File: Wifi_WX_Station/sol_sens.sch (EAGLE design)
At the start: 9 parts, among them IC1 MAX4330, U1 CPC1822

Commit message: updated BOM with all prices- As Checked in to BATCH PCB
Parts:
- C1: value 22nF -> 0.1uf
- C2: value 100nF -> 0.1uF
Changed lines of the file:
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@@
 <part name="R2" library="rcl" deviceset="R-US_" device="R0805" value="47K"/>
 <part name="IC1" library="Stofer" deviceset="MAX4330" device=""/>
-<part name="C2" library="rcl" deviceset="C-US" device="C0805" value="100nF"/>
-<part name="C1" library="rcl" deviceset="C-US" device="C0805" value="22nF"/>
+<part name="C2" library="rcl" deviceset="C-US" device="C0805" value="0.1uF"/>
+<part name="C1" library="rcl" deviceset="C-US" device="C0805" value="0.1uf"/>
 <part name="TP1" library="Stofer" deviceset="TP" device="B1,27"/>
 <part name="TP2" library="Stofer" deviceset="TP" device="B1,27"/>

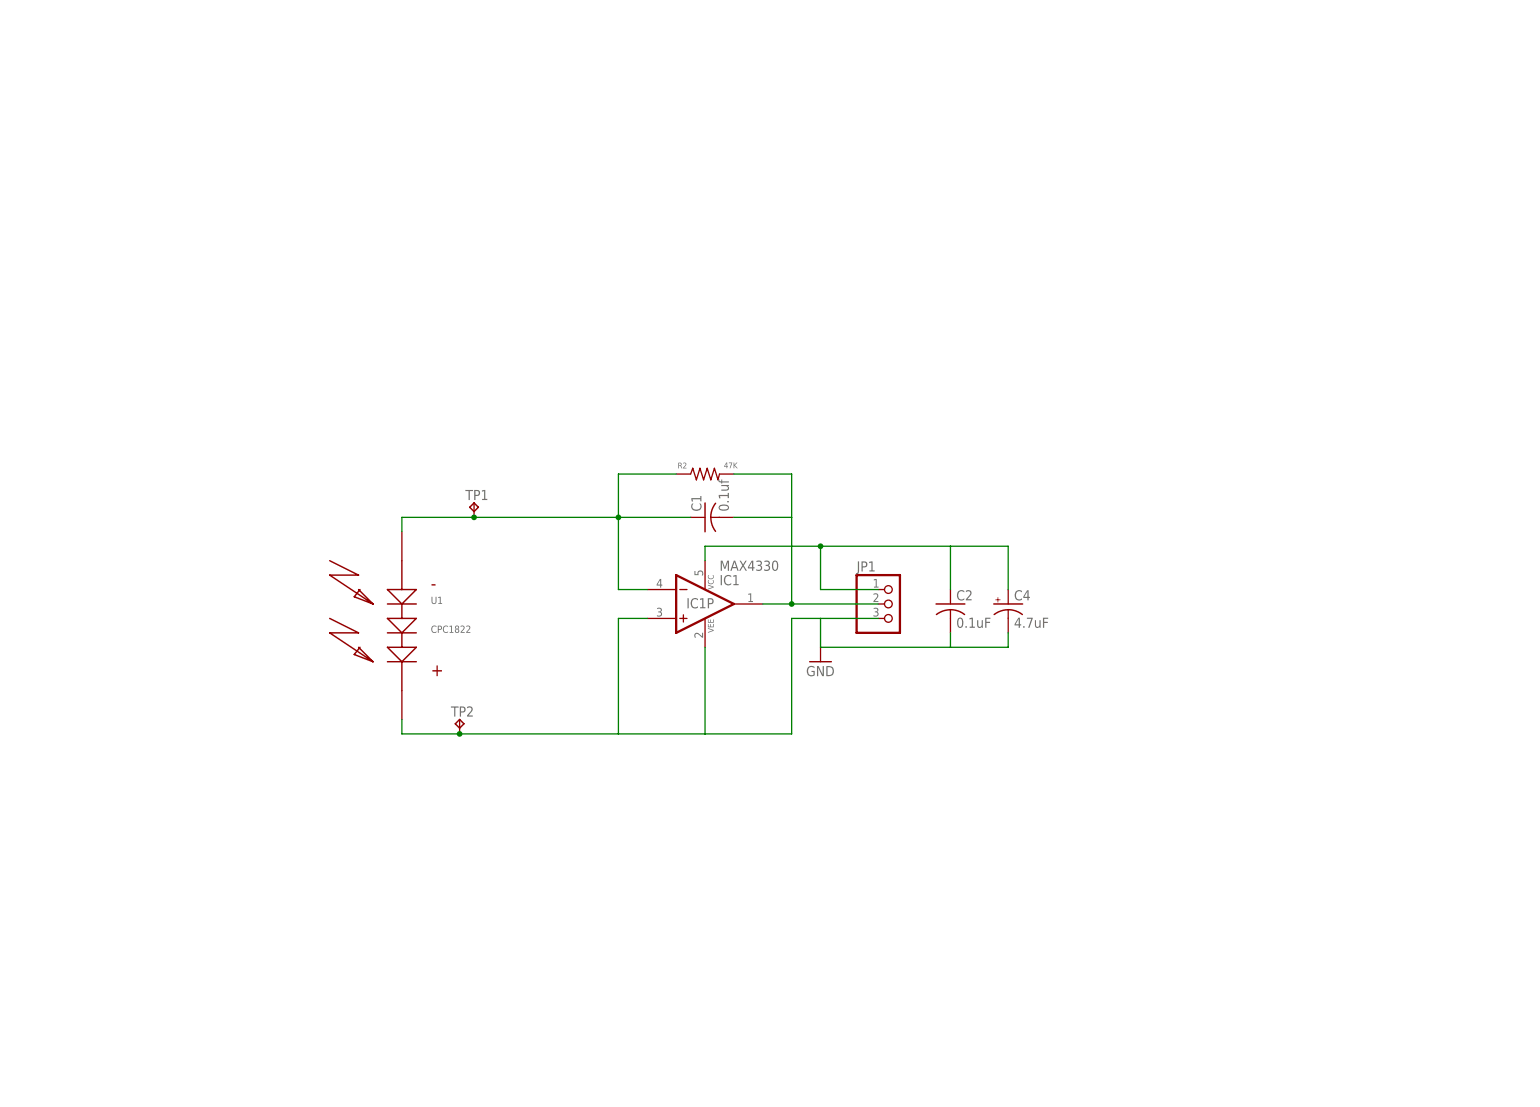
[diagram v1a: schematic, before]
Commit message: Added multiple new boards - H-pwrdist- Insp_Wind_enc, 5040 etc..
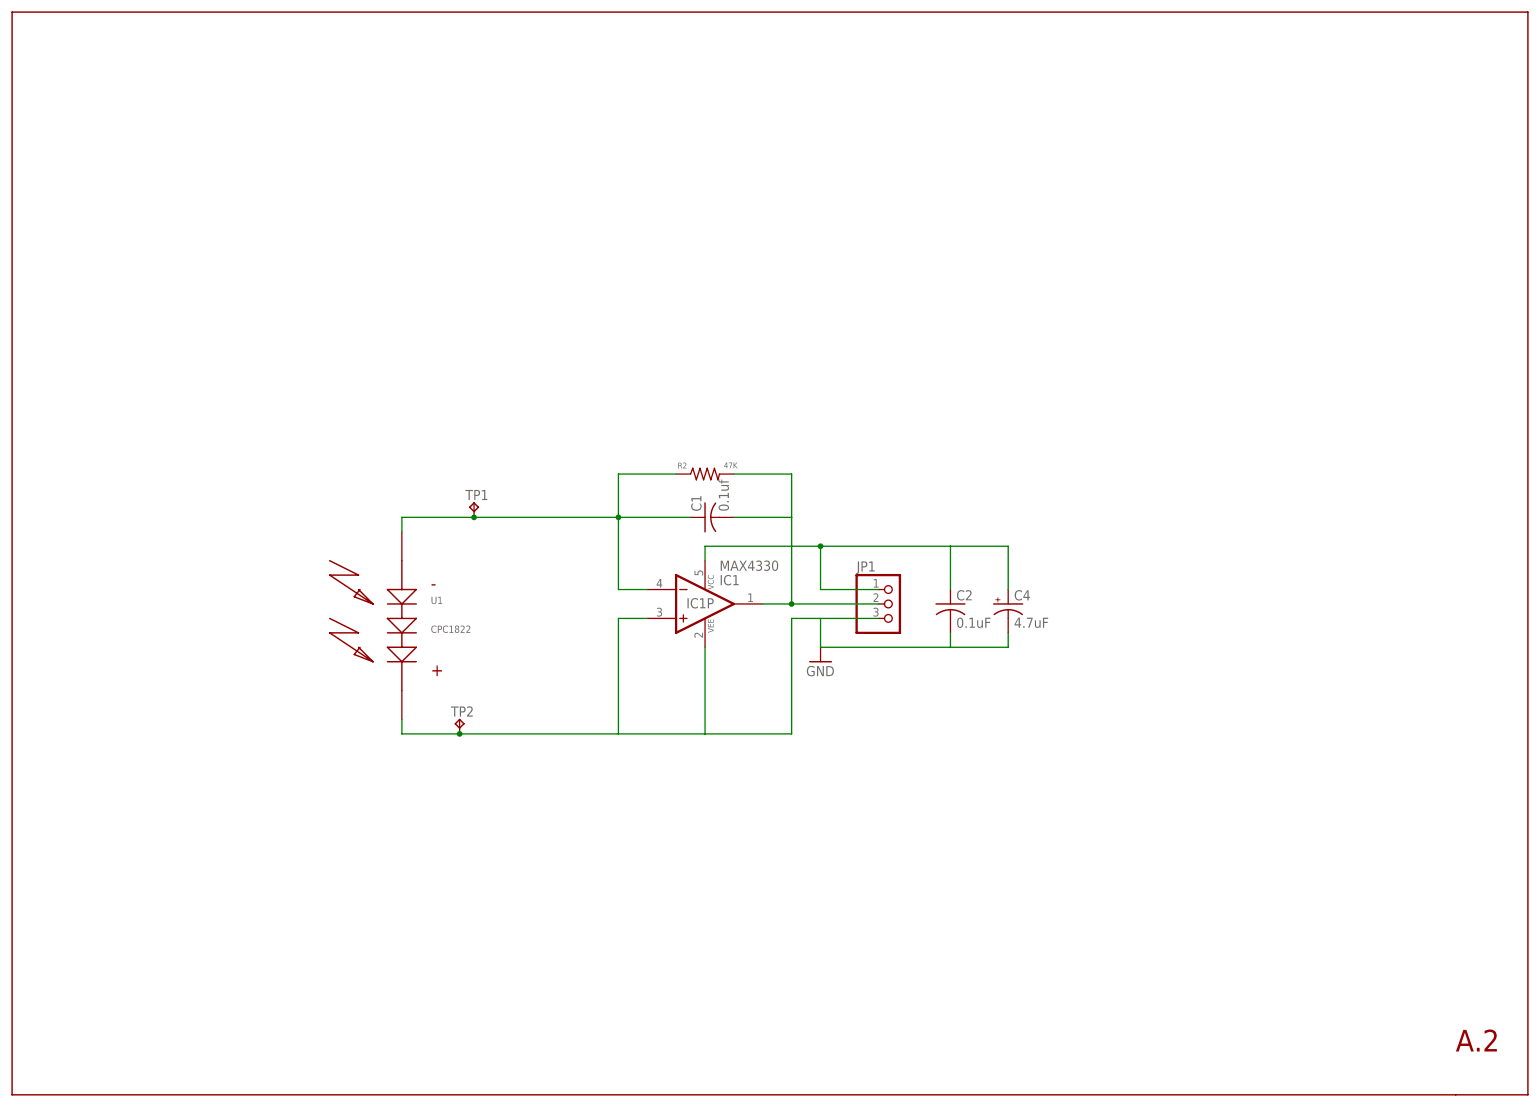
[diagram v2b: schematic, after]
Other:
- note added: "A.2"
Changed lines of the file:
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@@
 <part name="JP1" library="wifi_WX" deviceset="PINHD-1X3" device=""/>
 <part name="C4" library="rcl" deviceset="CPOL-US" device="R/2012-12R" value="4.7uF"/>
+<part name="U$1" library="1AA_Stofer" deviceset="8.5X11" device=""/>
 </parts>
 <sheets>
 <sheet>
 <plain>
+<text x="220.98" y="-22.86" size="3.81" layer="94">A.2</text>
 </plain>
 <instances>
@@
 <instance part="JP1" gate="A" x="121.92" y="55.88"/>
 <instance part="C4" gate="G$1" x="142.24" y="55.88"/>
+<instance part="U$1" gate="G$1" x="-33.02" y="-30.48"/>
+<instance part="U$1" gate="G$2" x="132.08" y="-30.48"/>
 </instances>
 <busses>
